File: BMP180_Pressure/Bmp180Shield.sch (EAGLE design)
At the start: 5 parts

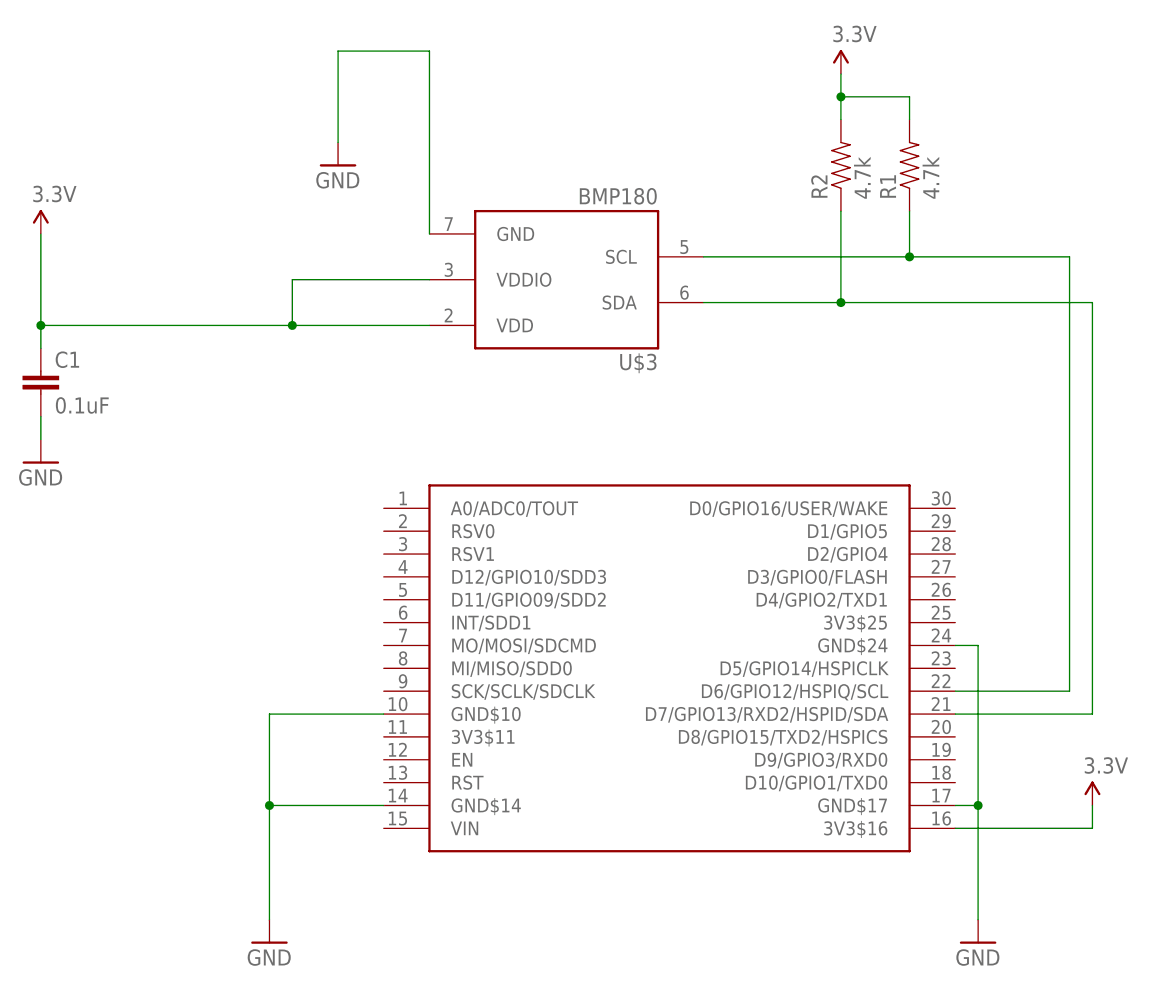
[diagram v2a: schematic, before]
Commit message: Updated the i2c pins to all shields to use d11/d12  as these pins will have dual use with the upcoming wifimcu Added FM24W256  Fram shield Added X95840 Digital potentiometer Shield Added AD5696 DAC Shield
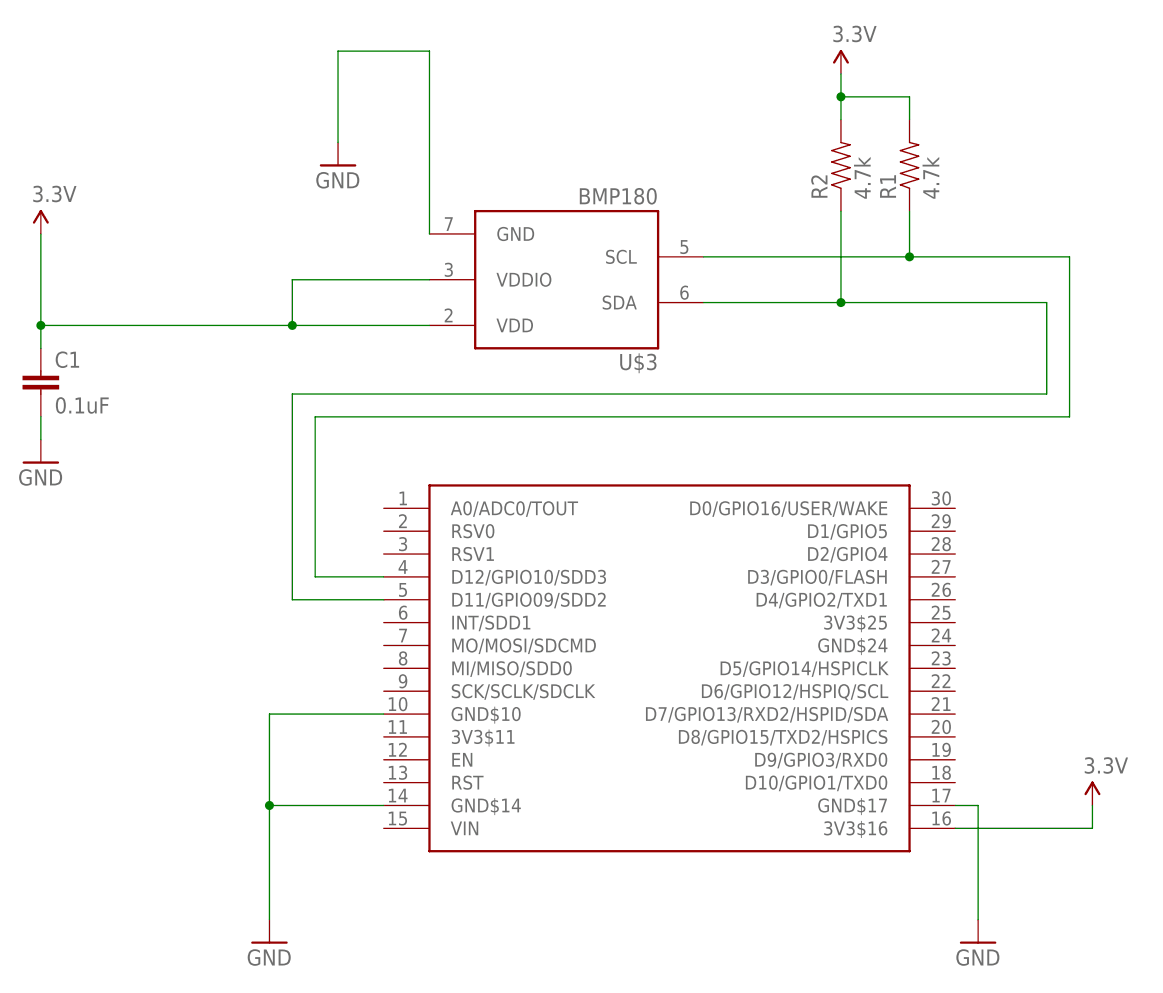
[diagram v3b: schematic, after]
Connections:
- net GND: no longer U$1.GND$24
- net N$2: now also U$1.D11/GPIO09/SDD2; no longer U$1.D7/GPIO13/RXD2/HSPID/SDA
- net N$3: now also U$1.D12/GPIO10/SDD3; no longer U$1.D6/GPIO12/HSPIQ/SCL
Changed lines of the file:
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@@
 <wire x1="71.12" y1="33.02" x2="73.66" y2="33.02" width="0.1524" layer="91"/>
 <wire x1="73.66" y1="33.02" x2="73.66" y2="20.32" width="0.1524" layer="91"/>
-<pinref part="U$1" gate="G$1" pin="GND$24"/>
-<wire x1="71.12" y1="50.8" x2="73.66" y2="50.8" width="0.1524" layer="91"/>
-<wire x1="73.66" y1="50.8" x2="73.66" y2="33.02" width="0.1524" layer="91"/>
-<junction x="73.66" y="33.02"/>
 </segment>
 </net>
@@
 <pinref part="R2" gate="G$1" pin="1"/>
 <wire x1="58.42" y1="88.9" x2="58.42" y2="99.06" width="0.1524" layer="91"/>
-<wire x1="58.42" y1="88.9" x2="86.36" y2="88.9" width="0.1524" layer="91"/>
-<wire x1="86.36" y1="88.9" x2="86.36" y2="43.18" width="0.1524" layer="91"/>
+<wire x1="58.42" y1="88.9" x2="81.28" y2="88.9" width="0.1524" layer="91"/>
+<wire x1="81.28" y1="88.9" x2="81.28" y2="78.74" width="0.1524" layer="91"/>
 <junction x="58.42" y="88.9"/>
-<pinref part="U$1" gate="G$1" pin="D7/GPIO13/RXD2/HSPID/SDA"/>
-<wire x1="86.36" y1="43.18" x2="71.12" y2="43.18" width="0.1524" layer="91"/>
 <pinref part="U$3" gate="G$1" pin="SDA"/>
 <wire x1="58.42" y1="88.9" x2="43.18" y2="88.9" width="0.1524" layer="91"/>
+<pinref part="U$1" gate="G$1" pin="D11/GPIO09/SDD2"/>
+<wire x1="7.62" y1="55.88" x2="-2.54" y2="55.88" width="0.1524" layer="91"/>
+<wire x1="-2.54" y1="55.88" x2="-2.54" y2="78.74" width="0.1524" layer="91"/>
+<wire x1="-2.54" y1="78.74" x2="81.28" y2="78.74" width="0.1524" layer="91"/>
 </segment>
 </net>
@@
 <wire x1="66.04" y1="93.98" x2="66.04" y2="99.06" width="0.1524" layer="91"/>
 <wire x1="66.04" y1="93.98" x2="83.82" y2="93.98" width="0.1524" layer="91"/>
-<wire x1="83.82" y1="93.98" x2="83.82" y2="45.72" width="0.1524" layer="91"/>
-<pinref part="U$1" gate="G$1" pin="D6/GPIO12/HSPIQ/SCL"/>
-<wire x1="83.82" y1="45.72" x2="71.12" y2="45.72" width="0.1524" layer="91"/>
+<wire x1="83.82" y1="93.98" x2="83.82" y2="76.2" width="0.1524" layer="91"/>
 <pinref part="U$3" gate="G$1" pin="SCL"/>
 <wire x1="66.04" y1="93.98" x2="43.18" y2="93.98" width="0.1524" layer="91"/>
 <junction x="66.04" y="93.98"/>
+<wire x1="83.82" y1="76.2" x2="0" y2="76.2" width="0.1524" layer="91"/>
+<wire x1="0" y1="76.2" x2="0" y2="58.42" width="0.1524" layer="91"/>
+<pinref part="U$1" gate="G$1" pin="D12/GPIO10/SDD3"/>
+<wire x1="0" y1="58.42" x2="7.62" y2="58.42" width="0.1524" layer="91"/>
 </segment>
 </net>
